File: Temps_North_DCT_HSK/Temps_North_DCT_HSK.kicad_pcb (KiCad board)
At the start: 2 copper layers, 53.3 x 57.1 mm, 7 parts, among them J1 North_Temps_1, J2 North_Temps_2, J3 Internal_Temps_DCT_HSK_Box_1, J4 Internal_Temps_DCT_HSK_Box_2

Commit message: See previous commit
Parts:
- added REF**: MountingHole_3.2mm_M3, MountingHole:MountingHole_3.2mm_M3, F.Cu at (122.2, 75.6)
- added REF**: MountingHole_3.2mm_M3, MountingHole:MountingHole_3.2mm_M3, F.Cu at (114.0, 75.6)
- moved G*** 0.22 mm to (128.9, 75.6)
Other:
- board text added: "Temps North Rev B Dennis H. Calderon 09/09/2023"
- board text removed: "Temps_North_DCT_HSK Dennis H. Calderon 10/21/2022"

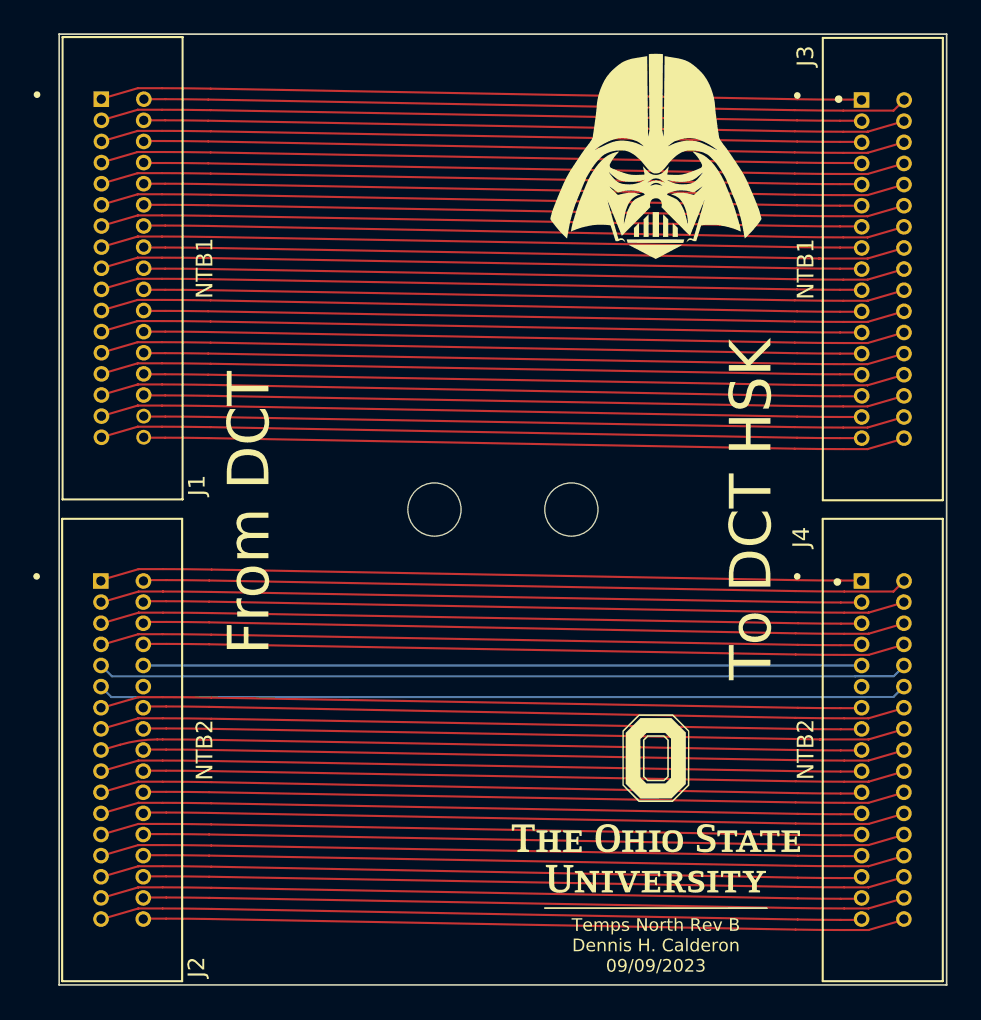
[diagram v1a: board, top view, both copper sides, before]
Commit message: Improved temperature PCBs that dont rely on small traces and meet all design rules. Also includes tuned routing for RTD channel.
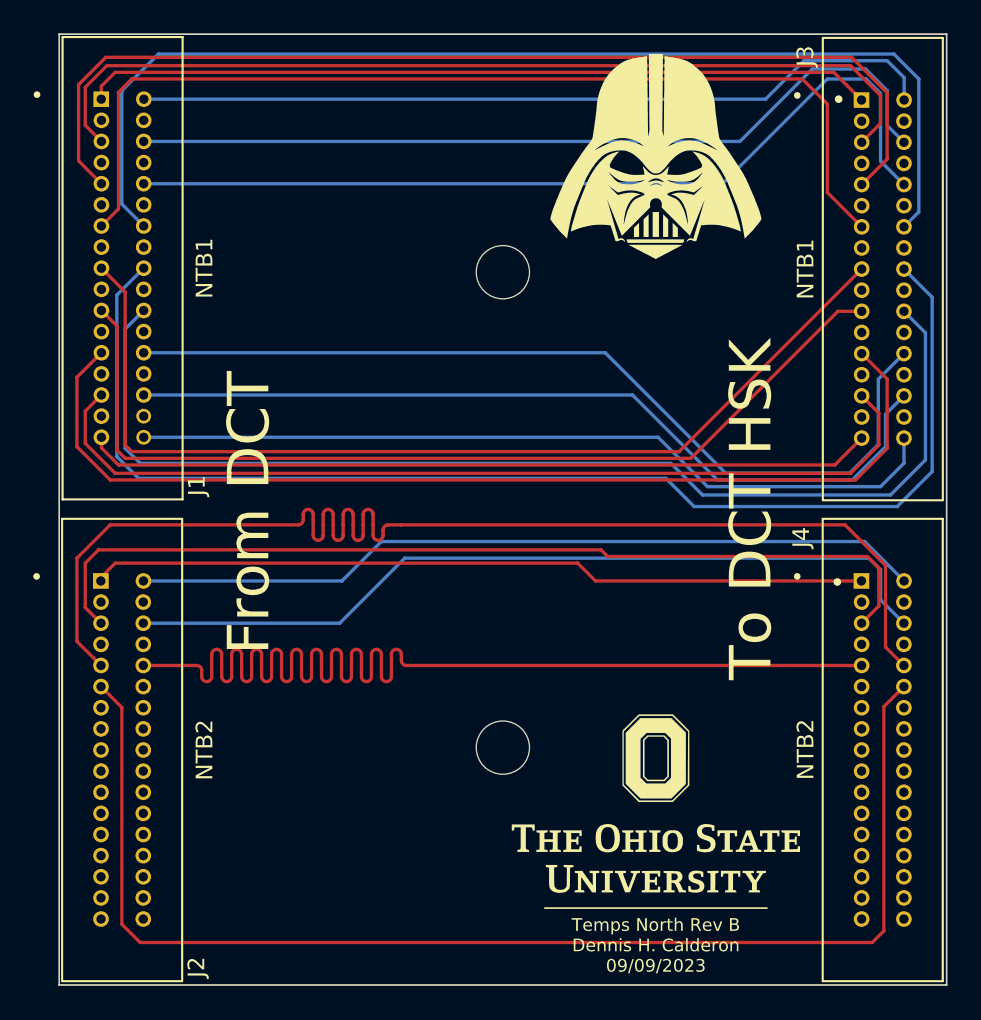
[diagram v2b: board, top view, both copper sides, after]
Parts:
- moved REF** 14.9 mm to (118.1, 89.9)
- moved REF** 14.8 mm to (118.1, 61.3)
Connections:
- net /TD1_1 renamed /TD1_1+
- net /TD1_2 renamed /TD1_1-
- J1 pad 11: /TD1_11 -> unconnected-(J1-Pin_11-Pad11)
- J1 pad 12: /TD1_12 -> unconnected-(J1-Pin_12-Pad12)
- J1 pad 15: /TD1_15 -> unconnected-(J1-Pin_15-Pad15)
- J1 pad 16: /TD1_16 -> unconnected-(J1-Pin_16-Pad16)
- J1 pad 19: /TD1_19 -> unconnected-(J1-Pin_19-Pad19)
- J1 pad 20: /TD1_20 -> unconnected-(J1-Pin_20-Pad20)
- J1 pad 23: /TD1_23 -> unconnected-(J1-Pin_23-Pad23)
- J1 pad 24: /TD1_24 -> unconnected-(J1-Pin_24-Pad24)
- J1 pad 27: /TD1_27 -> unconnected-(J1-Pin_27-Pad27)
- J1 pad 28: /TD1_28 -> unconnected-(J1-Pin_28-Pad28)
- J1 pad 3: /TD1_3 -> unconnected-(J1-Pin_3-Pad3)
- J1 pad 31: /TD1_31 -> unconnected-(J1-Pin_31-Pad31)
- J1 pad 32: /TD1_32 -> unconnected-(J1-Pin_32-Pad32)
- J1 pad 4: /TD1_4 -> unconnected-(J1-Pin_4-Pad4)
- J1 pad 7: /TD1_7 -> unconnected-(J1-Pin_7-Pad7)
- J1 pad 8: /TD1_8 -> unconnected-(J1-Pin_8-Pad8)
- J2 pad 13: /TD2_13 -> unconnected-(J2-Pin_13-Pad13)
- J2 pad 14: /TD2_14 -> unconnected-(J2-Pin_14-Pad14)
- J2 pad 15: /TD2_15 -> unconnected-(J2-Pin_15-Pad15)
- J2 pad 16: /TD2_16 -> unconnected-(J2-Pin_16-Pad16)
- J2 pad 17: /TD2_17 -> unconnected-(J2-Pin_17-Pad17)
- J2 pad 18: /TD2_18 -> unconnected-(J2-Pin_18-Pad18)
- J2 pad 19: /TD2_19 -> unconnected-(J2-Pin_19-Pad19)
- J2 pad 20: /TD2_20 -> unconnected-(J2-Pin_20-Pad20)
- J2 pad 21: /TD2_21 -> unconnected-(J2-Pin_21-Pad21)
- J2 pad 22: /TD2_22 -> unconnected-(J2-Pin_22-Pad22)
- J2 pad 23: /TD2_23 -> unconnected-(J2-Pin_23-Pad23)
- J2 pad 24: /TD2_24 -> unconnected-(J2-Pin_24-Pad24)
- J2 pad 25: /TD2_25 -> unconnected-(J2-Pin_25-Pad25)
- J2 pad 26: /TD2_26 -> unconnected-(J2-Pin_26-Pad26)
- J2 pad 27: /TD2_27 -> unconnected-(J2-Pin_27-Pad27)
- J2 pad 28: /TD2_28 -> unconnected-(J2-Pin_28-Pad28)
- J2 pad 29: /TD2_29 -> unconnected-(J2-Pin_29-Pad29)
- J2 pad 3: /TD2_3 -> unconnected-(J2-Pin_3-Pad3)
- J2 pad 30: /TD2_30 -> unconnected-(J2-Pin_30-Pad30)
- J2 pad 31: /TD2_31 -> unconnected-(J2-Pin_31-Pad31)
- J2 pad 32: /TD2_32 -> unconnected-(J2-Pin_32-Pad32)
- J2 pad 33: /TD2_33 -> unconnected-(J2-Pin_33-Pad33)
- J2 pad 34: /TD2_34 -> unconnected-(J2-Pin_34-Pad34)
- J2 pad 4: /TD2_4 -> unconnected-(J2-Pin_4-Pad4)
- J2 pad 7: /TD2_7 -> unconnected-(J2-Pin_7-Pad7)
- J2 pad 8: /TD2_8 -> unconnected-(J2-Pin_8-Pad8)
- J3 pad 11: /TD1_11 -> unconnected-(J3-Pin_11-Pad11)
- J3 pad 12: /TD1_12 -> unconnected-(J3-Pin_12-Pad12)
- J3 pad 15: /TD1_15 -> unconnected-(J3-Pin_15-Pad15)
- J3 pad 16: /TD1_16 -> unconnected-(J3-Pin_16-Pad16)
- J3 pad 19: /TD1_19 -> unconnected-(J3-Pin_19-Pad19)
- J3 pad 20: /TD1_20 -> unconnected-(J3-Pin_20-Pad20)
- J3 pad 23: /TD1_23 -> unconnected-(J3-Pin_23-Pad23)
- J3 pad 24: /TD1_24 -> unconnected-(J3-Pin_24-Pad24)
- J3 pad 27: /TD1_27 -> unconnected-(J3-Pin_27-Pad27)
- J3 pad 28: /TD1_28 -> unconnected-(J3-Pin_28-Pad28)
- J3 pad 3: /TD1_3 -> unconnected-(J3-Pin_3-Pad3)
- J3 pad 31: /TD1_31 -> unconnected-(J3-Pin_31-Pad31)
- J3 pad 32: /TD1_32 -> unconnected-(J3-Pin_32-Pad32)
- J3 pad 4: /TD1_4 -> unconnected-(J3-Pin_4-Pad4)
- J3 pad 7: /TD1_7 -> unconnected-(J3-Pin_7-Pad7)
- J3 pad 8: /TD1_8 -> unconnected-(J3-Pin_8-Pad8)
- J4 pad 13: /TD2_13 -> unconnected-(J4-Pin_13-Pad13)
- J4 pad 14: /TD2_14 -> unconnected-(J4-Pin_14-Pad14)
- J4 pad 15: /TD2_15 -> unconnected-(J4-Pin_15-Pad15)
- J4 pad 16: /TD2_16 -> unconnected-(J4-Pin_16-Pad16)
- J4 pad 17: /TD2_17 -> unconnected-(J4-Pin_17-Pad17)
- J4 pad 18: /TD2_18 -> unconnected-(J4-Pin_18-Pad18)
- J4 pad 19: /TD2_19 -> unconnected-(J4-Pin_19-Pad19)
- J4 pad 20: /TD2_20 -> unconnected-(J4-Pin_20-Pad20)
- J4 pad 21: /TD2_21 -> unconnected-(J4-Pin_21-Pad21)
- J4 pad 22: /TD2_22 -> unconnected-(J4-Pin_22-Pad22)
- J4 pad 23: /TD2_23 -> unconnected-(J4-Pin_23-Pad23)
- J4 pad 24: /TD2_24 -> unconnected-(J4-Pin_24-Pad24)
- J4 pad 25: /TD2_25 -> unconnected-(J4-Pin_25-Pad25)
- J4 pad 26: /TD2_26 -> unconnected-(J4-Pin_26-Pad26)
- J4 pad 27: /TD2_27 -> unconnected-(J4-Pin_27-Pad27)
- J4 pad 28: /TD2_28 -> unconnected-(J4-Pin_28-Pad28)
- J4 pad 29: /TD2_29 -> unconnected-(J4-Pin_29-Pad29)
- J4 pad 3: /TD2_3 -> unconnected-(J4-Pin_3-Pad3)
- J4 pad 30: /TD2_30 -> unconnected-(J4-Pin_30-Pad30)
- J4 pad 31: /TD2_31 -> unconnected-(J4-Pin_31-Pad31)
- J4 pad 32: /TD2_32 -> unconnected-(J4-Pin_32-Pad32)
- J4 pad 33: /TD2_33 -> unconnected-(J4-Pin_33-Pad33)
- J4 pad 34: /TD2_34 -> unconnected-(J4-Pin_34-Pad34)
- J4 pad 4: /TD2_4 -> unconnected-(J4-Pin_4-Pad4)
- J4 pad 7: /TD2_7 -> unconnected-(J4-Pin_7-Pad7)
- J4 pad 8: /TD2_8 -> unconnected-(J4-Pin_8-Pad8)
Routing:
- net /TD1_16: track 45.8 -> 0.00 mm
- net /TD2_16: track 45.8 -> 0.00 mm
- net /TD2_21: track 45.8 -> 0.00 mm
- net /TD2_14: track 45.8 -> 0.00 mm
- net /TD1_23: track 45.8 -> 0.00 mm
- net /TD2_23: track 45.8 -> 0.00 mm
- net /TD2_25: track 45.8 -> 0.00 mm
- net /TD1_12: track 45.8 -> 0.00 mm
- net /TD2_18: track 45.8 -> 0.00 mm
- net /TD1_20: track 45.8 -> 0.00 mm
- net /TD2_7: track 45.8 -> 0.00 mm
- net /TD1_7: track 45.8 -> 0.00 mm
- net /TD1_28: track 45.8 -> 0.00 mm
- net /TD2_28: track 45.8 -> 0.00 mm
- net /TD2_15: track 45.8 -> 0.00 mm
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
